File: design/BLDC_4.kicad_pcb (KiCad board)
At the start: 2 copper layers, 127 parts, among them K1 SERVO, P1 HALL, P10 CONN_DRV, P101 CANBUS, P11 CONN_DRV, P12 CONN_DRV, P13 CONN_DRV, P14 CONN_DRV, P15 CONN_DRV, P16 CONN_DRV, P17 CONN_DRV, P18 CONN_DRV, P2 SWD, P3 PWR_COMM/USART1/Encoder, P4 IN+, P5 IN-, P6 CONN_DRV, P7 CONN_DRV, P8 Current sensors, P9 CONN_DRV, U1 STM32F40X_LQFP64, U2 ISO1050, U3 IRS2184, U4 IRS2184, U5 IRS2184, U6 NCP1117ST33T3G, X1 MINI-USB-SHIELD-32005-201, X2 8MHz 10ppm

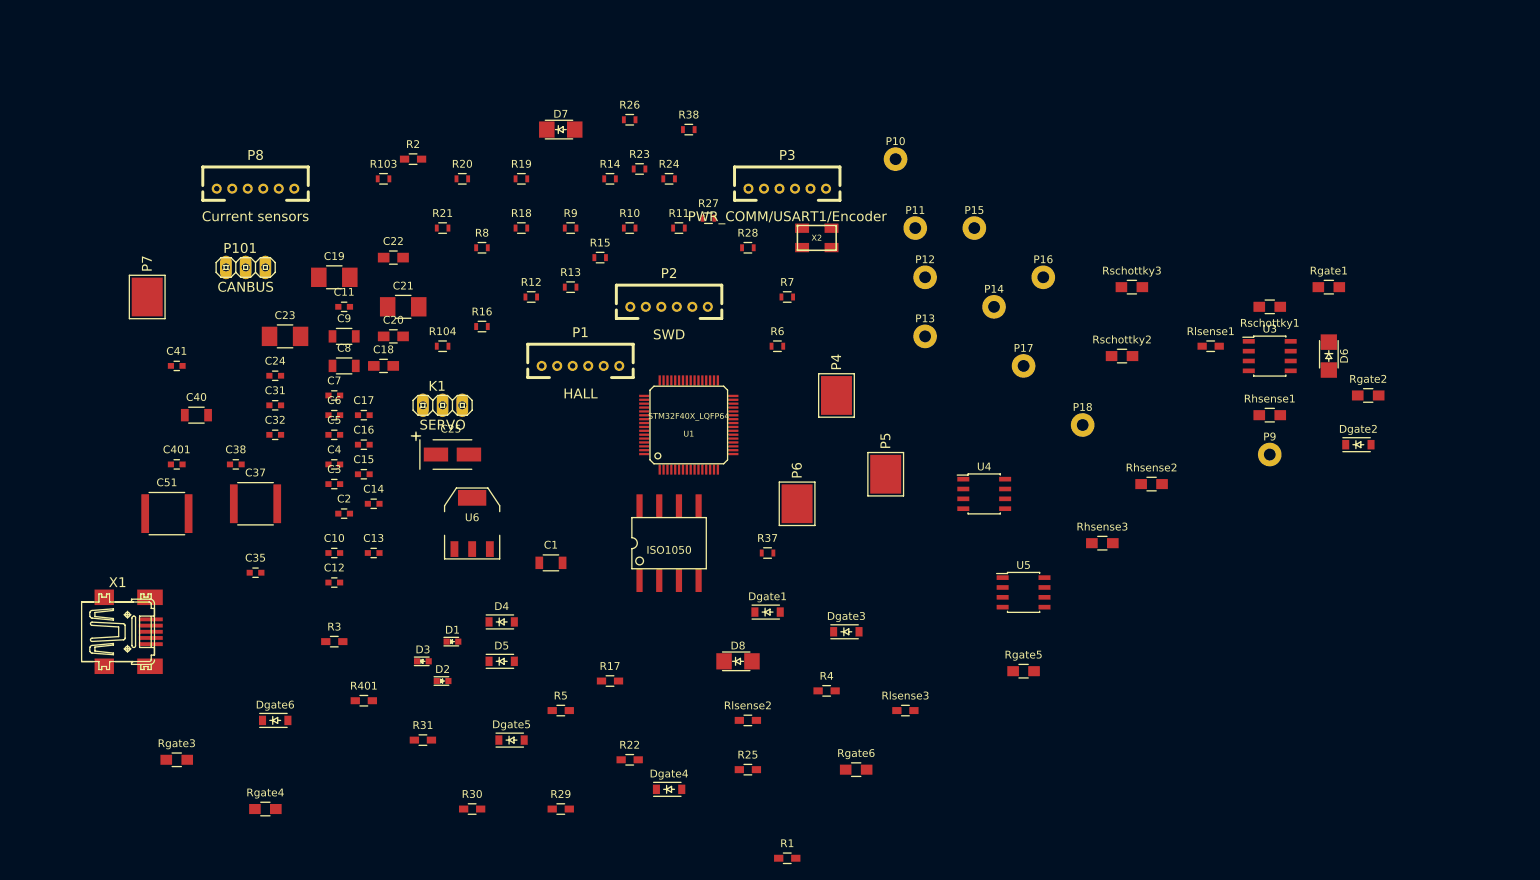
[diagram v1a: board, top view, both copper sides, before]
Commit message: Arranged some parts.
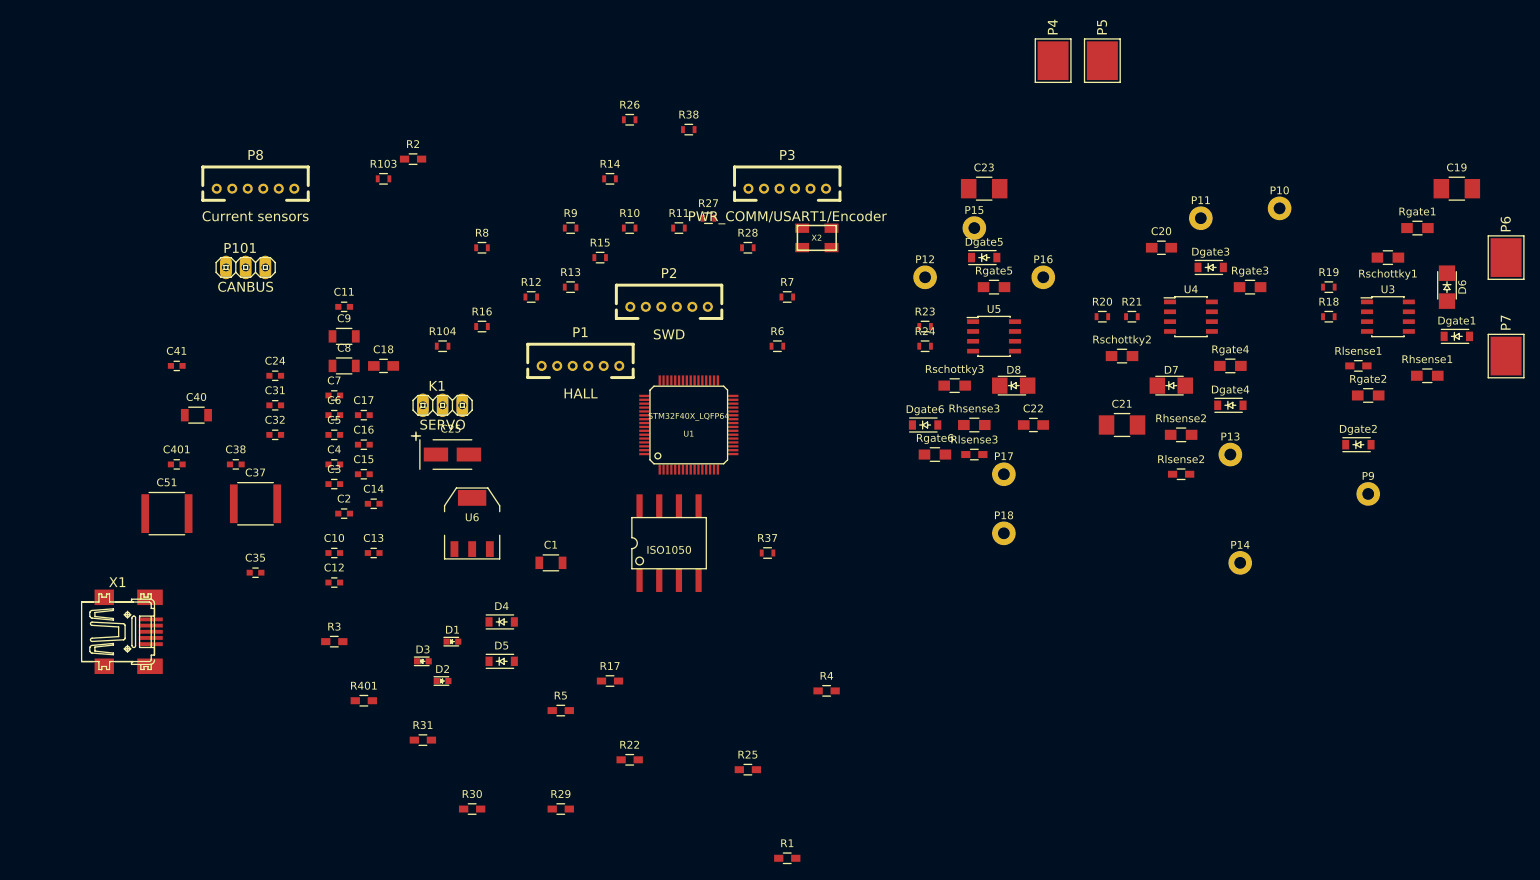
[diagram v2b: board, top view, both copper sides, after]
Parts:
- moved P7 175.4 mm to (270.5, 91.4)
- moved Rgate3 151.3 mm to (237.5, 82.5)
- moved C19 145.2 mm to (264.2, 69.8)
- moved Rgate4 137.0 mm to (234.9, 92.7)
- moved R19 105.1 mm to (247.7, 82.5)
- moved R18 104.8 mm to (247.7, 86.4)
- moved C20 99.7 mm to (226.1, 77.5)
- moved P6 96.8 mm to (270.5, 78.7)
- moved Dgate1 95.7 mm to (264.2, 88.9)
- moved C21 94.0 mm to (221.0, 100.3)
- moved C23 92.2 mm to (203.2, 69.8)
- moved Dgate6 92.1 mm to (195.6, 100.3)
- moved R21 89.6 mm to (222.2, 86.4)
- moved Dgate4 87.7 mm to (234.9, 97.8)
- moved Dgate5 87.1 mm to (203.2, 78.7)
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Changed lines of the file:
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@@
     (links 242)
     (no_connects 242)
-    (area 0 0 0 0)
+    (area 76.651025 57.935 264.076971 159.085)
     (thickness 1.6)
     (drawings 0)
@@
     (pad_to_mask_clearance 0)
     (aux_axis_origin 0 0)
-    (visible_elements FFFFFF7F)
+    (visible_elements FFFFF77F)
     (pcbplotparams
       (layerselection 0x00030_80000001)
@@
   )
   (module Capacitors_SMD:C_1210_HandSoldering (layer F.Cu)
-    (at 119.38 81.28)
+    (at 264.16 69.85)
     (descr "Capacitor SMD 1210, hand soldering")
     (tags "capacitor 1210")
@@
   )
   (module Capacitors_SMD:C_0805_HandSoldering (layer F.Cu)
-    (at 127 88.9)
+    (at 226.06 77.47)
     (descr "Capacitor SMD 0805, hand soldering")
     (tags "capacitor 0805")
@@
   )
   (module Capacitors_SMD:C_1210_HandSoldering (layer F.Cu)
-    (at 128.27 85.09)
+    (at 220.98 100.33)
     (descr "Capacitor SMD 1210, hand soldering")
     (tags "capacitor 1210")
@@
   )
   (module Capacitors_SMD:C_0805_HandSoldering (layer F.Cu)
-    (at 127 78.74)
+    (at 209.55 100.33)
     (descr "Capacitor SMD 0805, hand soldering")
     (tags "capacitor 0805")
@@
   )
   (module Capacitors_SMD:C_1210_HandSoldering (layer F.Cu)
-    (at 113.03 88.9)
+    (at 203.2 69.85)
     (descr "Capacitor SMD 1210, hand soldering")
     (tags "capacitor 1210")
@@
   )
   (module FootprintsBLDC:DO-214AC_SOD-123 (layer F.Cu)
-    (at 247.65 91.44 270)
+    (at 262.89 82.55 270)
     (descr DO-214AC_SOD-123)
     (tags SOD-123)
@@
   )
   (module FootprintsBLDC:DO-214AC_SOD-123 (layer F.Cu)
-    (at 148.59 62.23)
+    (at 227.33 95.25)
     (descr DO-214AC_SOD-123)
     (tags SOD-123)
@@
   )
   (module FootprintsBLDC:DO-214AC_SOD-123 (layer F.Cu)
-    (at 171.45 130.81)
+    (at 207.01 95.25)
     (descr DO-214AC_SOD-123)
     (tags SOD-123)
@@
   )
   (module Diodes_SMD:SOD-123 (layer F.Cu)
-    (at 175.26 124.46)
+    (at 264.16 88.9)
     (descr SOD-123)
     (tags SOD-123)
@@
   )
   (module Diodes_SMD:SOD-123 (layer F.Cu)
-    (at 185.42 127)
+    (at 232.41 80.01)
     (descr SOD-123)
     (tags SOD-123)
@@
   )
   (module Diodes_SMD:SOD-123 (layer F.Cu)
-    (at 162.56 147.32)
+    (at 234.95 97.79)
     (descr SOD-123)
     (tags SOD-123)
@@
   )
   (module Diodes_SMD:SOD-123 (layer F.Cu)
-    (at 142.24 140.97)
+    (at 203.2 78.74)
     (descr SOD-123)
     (tags SOD-123)
@@
   )
   (module Diodes_SMD:SOD-123 (layer F.Cu)
-    (at 111.76 138.43)
+    (at 195.58 100.33)
     (descr SOD-123)
     (tags SOD-123)
@@
   )
   (module CRF1:1PAD_4x5mm (layer F.Cu)
-    (at 184.15 96.52)
+    (at 212.09 53.34)
     (fp_text reference P4 (at 0 -4.3 270) (layer F.SilkS)
       (effects (font (thickness 0.3048)))
@@
   )
   (module CRF1:1PAD_4x5mm (layer F.Cu)
-    (at 190.5 106.68)
+    (at 218.44 53.34)
     (fp_text reference P5 (at 0 -4.3 270) (layer F.SilkS)
       (effects (font (thickness 0.3048)))
@@
   )
   (module CRF1:1PAD_4x5mm (layer F.Cu)
-    (at 179.07 110.49)
+    (at 270.51 78.74)
     (fp_text reference P6 (at 0 -4.3 270) (layer F.SilkS)
       (effects (font (thickness 0.3048)))
@@
   )
   (module CRF1:1PAD_4x5mm (layer F.Cu)
-    (at 95.25 83.82)
+    (at 270.51 91.44)
     (fp_text reference P7 (at 0 -4.3 270) (layer F.SilkS)
       (effects (font (thickness 0.3048)))
@@
   )
   (module FootprintsBLDC:PAD_DRV (layer F.Cu)
-    (at 240.03 104.14)
+    (at 252.73 109.22)
     (descr "module 1 pin (ou trou mecanique de percage)")
     (tags DEV)
@@
   )
   (module FootprintsBLDC:PAD_DRV (layer F.Cu)
-    (at 191.77 66.04)
+    (at 241.3 72.39)
     (descr "module 1 pin (ou trou mecanique de percage)")
     (tags DEV)
@@
   )
   (module FootprintsBLDC:PAD_DRV (layer F.Cu)
-    (at 194.31 74.93)
+    (at 231.14 73.66)
     (descr "module 1 pin (ou trou mecanique de percage)")
     (tags DEV)
@@
   )
   (module FootprintsBLDC:PAD_DRV (layer F.Cu)
-    (at 195.58 88.9)
+    (at 234.95 104.14)
     (descr "module 1 pin (ou trou mecanique de percage)")
     (tags DEV)
@@
   )
   (module FootprintsBLDC:PAD_DRV (layer F.Cu)
-    (at 204.47 85.09)
+    (at 236.22 118.11)
     (descr "module 1 pin (ou trou mecanique de percage)")
     (tags DEV)
@@
   )
   (module FootprintsBLDC:PAD_DRV (layer F.Cu)
-    (at 208.28 92.71)
+    (at 205.74 106.68)
     (descr "module 1 pin (ou trou mecanique de percage)")
     (tags DEV)
@@
   )
   (module FootprintsBLDC:PAD_DRV (layer F.Cu)
-    (at 215.9 100.33)
+    (at 205.74 114.3)
     (descr "module 1 pin (ou trou mecanique de percage)")
     (tags DEV)
@@
   )
   (module Resistors_SMD:R_0603 (layer F.Cu)
-    (at 143.51 74.93)
+    (at 247.65 86.36)
     (descr "Resistor SMD 0603, reflow soldering, Vishay (see dcrcw.pdf)")
     (tags "resistor 0603")
@@
   )
   (module Resistors_SMD:R_0603 (layer F.Cu)
-    (at 143.51 68.58)
+    (at 247.65 82.55)
     (descr "Resistor SMD 0603, reflow soldering, Vishay (see dcrcw.pdf)")
     (tags "resistor 0603")
@@
   )
   (module Resistors_SMD:R_0603 (layer F.Cu)
-    (at 135.89 68.58)
+    (at 218.44 86.36)
     (descr "Resistor SMD 0603, reflow soldering, Vishay (see dcrcw.pdf)")
     (tags "resistor 0603")
@@
   )
   (module Resistors_SMD:R_0603 (layer F.Cu)
-    (at 133.35 74.93)
+    (at 222.25 86.36)
     (descr "Resistor SMD 0603, reflow soldering, Vishay (see dcrcw.pdf)")
     (tags "resistor 0603")
@@
   )
   (module Resistors_SMD:R_0603 (layer F.Cu)
-    (at 158.75 67.31)
+    (at 195.58 87.63)
     (descr "Resistor SMD 0603, reflow soldering, Vishay (see dcrcw.pdf)")
     (tags "resistor 0603")
@@
   )
   (module Resistors_SMD:R_0603 (layer F.Cu)
-    (at 162.56 68.58)
+    (at 195.58 90.17)
     (descr "Resistor SMD 0603, reflow soldering, Vishay (see dcrcw.pdf)")
     (tags "resistor 0603")
@@
   )
   (module Resistors_SMD:R_0805_HandSoldering (layer F.Cu)
-    (at 247.65 82.55)
+    (at 259.08 74.93)
     (descr "Resistor SMD 0805, hand soldering")
     (tags "resistor 0805")
@@
   )
   (module Resistors_SMD:R_0805_HandSoldering (layer F.Cu)
-    (at 99.06 143.51)
+    (at 237.49 82.55)
     (descr "Resistor SMD 0805, hand soldering")
     (tags "resistor 0805")
@@
   )
   (module Resistors_SMD:R_0805_HandSoldering (layer F.Cu)
-    (at 110.49 149.86)
+    (at 234.95 92.71)
     (descr "Resistor SMD 0805, hand soldering")
     (tags "resistor 0805")
@@
   )
   (module Resistors_SMD:R_0805_HandSoldering (layer F.Cu)
-    (at 208.28 132.08)
+    (at 204.47 82.55)
     (descr "Resistor SMD 0805, hand soldering")
     (tags "resistor 0805")
@@
   )
   (module Resistors_SMD:R_0805_HandSoldering (layer F.Cu)
-    (at 186.69 144.78)
+    (at 196.85 104.14)
     (descr "Resistor SMD 0805, hand soldering")
     (tags "resistor 0805")
@@
   )
   (module Resistors_SMD:R_0805_HandSoldering (layer F.Cu)
-    (at 240.03 99.06)
+    (at 260.35 93.98)
     (descr "Resistor SMD 0805, hand soldering")
     (tags "resistor 0805")
@@
   )
   (module Resistors_SMD:R_0805_HandSoldering (layer F.Cu)
-    (at 224.79 107.95)
+    (at 228.6 101.6)
     (descr "Resistor SMD 0805, hand soldering")
     (tags "resistor 0805")
@@
   )
   (module Resistors_SMD:R_0805_HandSoldering (layer F.Cu)
-    (at 218.44 115.57)
+    (at 201.93 100.33)
     (descr "Resistor SMD 0805, hand soldering")
     (tags "resistor 0805")
@@
   )
   (module Resistors_SMD:R_0603_HandSoldering (layer F.Cu)
-    (at 232.41 90.17)
+    (at 251.46 92.71)
     (descr "Resistor SMD 0603, hand soldering")
     (tags "resistor 0603")
@@
   )
   (module Resistors_SMD:R_0603_HandSoldering (layer F.Cu)
-    (at 172.72 138.43)
+    (at 228.6 106.68)
     (descr "Resistor SMD 0603, hand soldering")
     (tags "resistor 0603")
@@
   )
   (module Resistors_SMD:R_0603_HandSoldering (layer F.Cu)
-    (at 193.04 137.16)
+    (at 201.93 104.14)
     (descr "Resistor SMD 0603, hand soldering")
     (tags "resistor 0603")
@@
   )
   (module Resistors_SMD:R_0805_HandSoldering (layer F.Cu)
-    (at 240.03 85.09 180)
+    (at 255.27 78.74 180)
     (descr "Resistor SMD 0805, hand soldering")
     (tags "resistor 0805")
@@
   )
   (module Resistors_SMD:R_0805_HandSoldering (layer F.Cu)
-    (at 222.25 82.55)
+    (at 199.39 95.25)
     (descr "Resistor SMD 0805, hand soldering")
     (tags "resistor 0805")
@@
   )
   (module Housings_SOIC:SOIC-8_3.9x4.9mm_Pitch1.27mm (layer F.Cu)
-    (at 240.03 91.44)
+    (at 255.27 86.36)
     (descr "8-Lead Plastic Small Outline (SN) - Narrow, 3.90 mm Body [SOIC] (see Microchip Packaging Specification 00000049BS.pdf)")
     (tags "SOIC 1.27")
@@
   )
   (module Housings_SOIC:SOIC-8_3.9x4.9mm_Pitch1.27mm (layer F.Cu)
-    (at 203.2 109.22)
+    (at 229.87 86.36)
     (descr "8-Lead Plastic Small Outline (SN) - Narrow, 3.90 mm Body [SOIC] (see Microchip Packaging Specification 00000049BS.pdf)")
     (tags "SOIC 1.27")
@@
   )
   (module Housings_SOIC:SOIC-8_3.9x4.9mm_Pitch1.27mm (layer F.Cu)
-    (at 208.28 121.92)
+    (at 204.47 88.9)
     (descr "8-Lead Plastic Small Outline (SN) - Narrow, 3.90 mm Body [SOIC] (see Microchip Packaging Specification 00000049BS.pdf)")
     (tags "SOIC 1.27")
